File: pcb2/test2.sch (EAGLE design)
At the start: 56 parts, among them IC1 LMV358M, IC2 LMV358M, IC3 STM32F10XCXT6, Q1 8mhz

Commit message: ready to facturing
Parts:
- C-ADCBATT: value (none) -> 100nf
- C-CLK1, C-CLK2: value (none) -> 22pf
- R-ADCBATT2: value 4k7 -> 1k5
- R-ADCLAMP1, R-ADCLAMP2, R-ADCLAMP3, R-ADCPV1, R-ADCPV2, R-ADCPV3, R-ADCUSB1, R-ADCUSB2, R-ADCUSB3: value 4k7 -> 100k
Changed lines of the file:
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@@
 <part name="C-USB2" library="resistor" deviceset="CPOL-EU" device="E2.5-5" value="220uF"/>
 <part name="IC1" library="linear" deviceset="LMV358?*" device="M"/>
-<part name="R-ADCPV2" library="resistor" deviceset="R-EU_" device="R0805" value="4k7"/>
-<part name="R-ADCPV1" library="resistor" deviceset="R-EU_" device="R0805" value="4k7"/>
-<part name="R-ADCPV3" library="resistor" deviceset="R-EU_" device="R0805" value="4k7"/>
+<part name="R-ADCPV2" library="resistor" deviceset="R-EU_" device="R0805" value="100k"/>
+<part name="R-ADCPV1" library="resistor" deviceset="R-EU_" device="R0805" value="100k"/>
+<part name="R-ADCPV3" library="resistor" deviceset="R-EU_" device="R0805" value="100k"/>
 <part name="D-PV1" library="diode" deviceset="DIODE-" device="DO-214AC"/>
 <part name="IC2" library="linear" deviceset="LMV358?*" device="M"/>
-<part name="R-ADCLAMP2" library="resistor" deviceset="R-EU_" device="R0805" value="4k7"/>
-<part name="R-ADCLAMP1" library="resistor" deviceset="R-EU_" device="R0805" value="4k7"/>
-<part name="R-ADCLAMP3" library="resistor" deviceset="R-EU_" device="R0805" value="4k7"/>
+<part name="R-ADCLAMP2" library="resistor" deviceset="R-EU_" device="R0805" value="100k"/>
+<part name="R-ADCLAMP1" library="resistor" deviceset="R-EU_" device="R0805" value="100k"/>
+<part name="R-ADCLAMP3" library="resistor" deviceset="R-EU_" device="R0805" value="100k"/>
 <part name="D-LAMP1" library="diode" deviceset="DIODE-" device="DO-214AC"/>
-<part name="R-ADCUSB1" library="resistor" deviceset="R-EU_" device="R0805" value="4k7"/>
-<part name="R-ADCUSB2" library="resistor" deviceset="R-EU_" device="R0805" value="4k7"/>
-<part name="R-ADCUSB3" library="resistor" deviceset="R-EU_" device="R0805" value="4k7"/>
+<part name="R-ADCUSB1" library="resistor" deviceset="R-EU_" device="R0805" value="100k"/>
+<part name="R-ADCUSB2" library="resistor" deviceset="R-EU_" device="R0805" value="100k"/>
+<part name="R-ADCUSB3" library="resistor" deviceset="R-EU_" device="R0805" value="100k"/>
 <part name="D-USB1" library="diode" deviceset="DIODE-" device="DO-214AC"/>
 <part name="LED1" library="led" deviceset="LED" device="CHIP-LED0805"/>
@@
 <part name="LED6" library="led" deviceset="LED" device="CHIP-LED0805"/>
 <part name="R-ADCBATT1" library="resistor" deviceset="R-EU_" device="R0805" value="4k7"/>
-<part name="R-ADCBATT2" library="resistor" deviceset="R-EU_" device="R0805" value="4k7"/>
-<part name="C-ADCBATT" library="resistor" deviceset="C-EU" device="C0805"/>
+<part name="R-ADCBATT2" library="resistor" deviceset="R-EU_" device="R0805" value="1k5"/>
+<part name="C-ADCBATT" library="resistor" deviceset="C-EU" device="C0805" value="100nf"/>
 <part name="S-NRST" library="switch" deviceset="SKHMP*E010" device="" technology="S"/>
 <part name="R-NRST" library="resistor" deviceset="R-EU_" device="R0805" value="4k7"/>
@@
 <part name="JP1" library="pinhead" deviceset="PINHD-1X3" device=""/>
 <part name="Q1" library="crystal" deviceset="CRYSTAL" device="HC49S" value="8mhz"/>
-<part name="C-CLK1" library="resistor" deviceset="C-EU" device="C0805"/>
-<part name="C-CLK2" library="resistor" deviceset="C-EU" device="C0805"/>
+<part name="C-CLK1" library="resistor" deviceset="C-EU" device="C0805" value="22pf"/>
+<part name="C-CLK2" library="resistor" deviceset="C-EU" device="C0805" value="22pf"/>
 <part name="FLASH" library="pinhead" deviceset="PINHD-1X4" device=""/>
 <part name="X1" library="con-berg" deviceset="PN87520" device=""/>

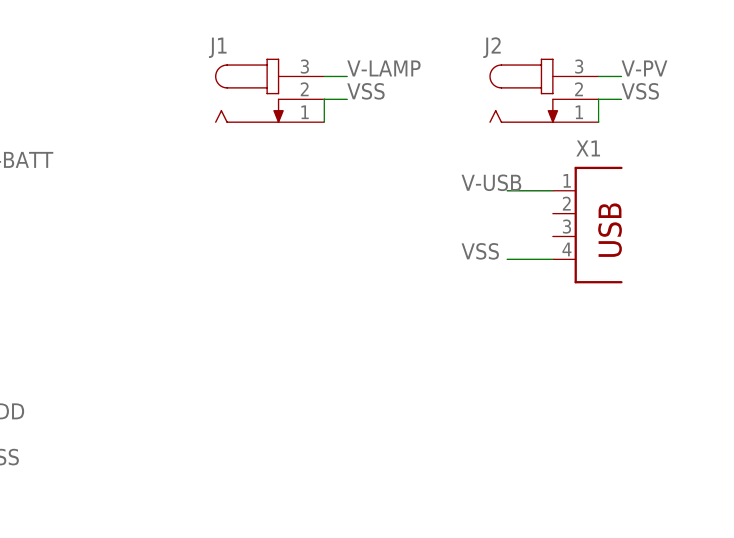
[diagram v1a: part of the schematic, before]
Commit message: add mount holes
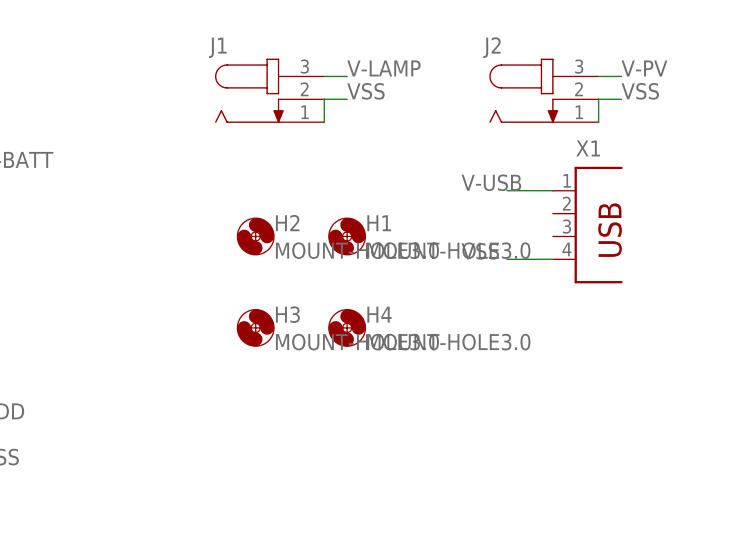
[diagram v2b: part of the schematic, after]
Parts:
- added H1, H2, H3, H4: MOUNT-HOLE3.0, holes:MOUNT-HOLE3.0
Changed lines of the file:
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@@
 <part name="R-CON-PV" library="resistor" deviceset="R-EU_" device="R0805" value="4k7"/>
 <part name="R-CONUSB" library="resistor" deviceset="R-EU_" device="R0805" value="4k7"/>
+<part name="H1" library="holes" deviceset="MOUNT-HOLE" device="3.0"/>
+<part name="H2" library="holes" deviceset="MOUNT-HOLE" device="3.0"/>
+<part name="H3" library="holes" deviceset="MOUNT-HOLE" device="3.0"/>
+<part name="H4" library="holes" deviceset="MOUNT-HOLE" device="3.0"/>
 </parts>
 <sheets>
@@
 <instance part="R-CON-PV" gate="G$1" x="25.4" y="53.34" rot="R90"/>
 <instance part="R-CONUSB" gate="G$1" x="25.4" y="-63.5" rot="R90"/>
+<instance part="H1" gate="G$1" x="172.72" y="-60.96"/>
+<instance part="H2" gate="G$1" x="162.56" y="-60.96"/>
+<instance part="H3" gate="G$1" x="162.56" y="-71.12"/>
+<instance part="H4" gate="G$1" x="172.72" y="-71.12"/>
 </instances>
 <busses>
